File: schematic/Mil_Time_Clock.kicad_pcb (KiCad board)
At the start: 2 copper layers, 188.8 x 102.5 mm, 106 parts, among them J1 Conn_01x27, J2 Speaker_Conn_01x02, J3 Barrel_Jack_Switch, J4 Conn_01x27, Q1 2N3904, Q2 2N3904, Q3 2N3904, Q4 2N3904, Q5 2N3904, U1 SM420561N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

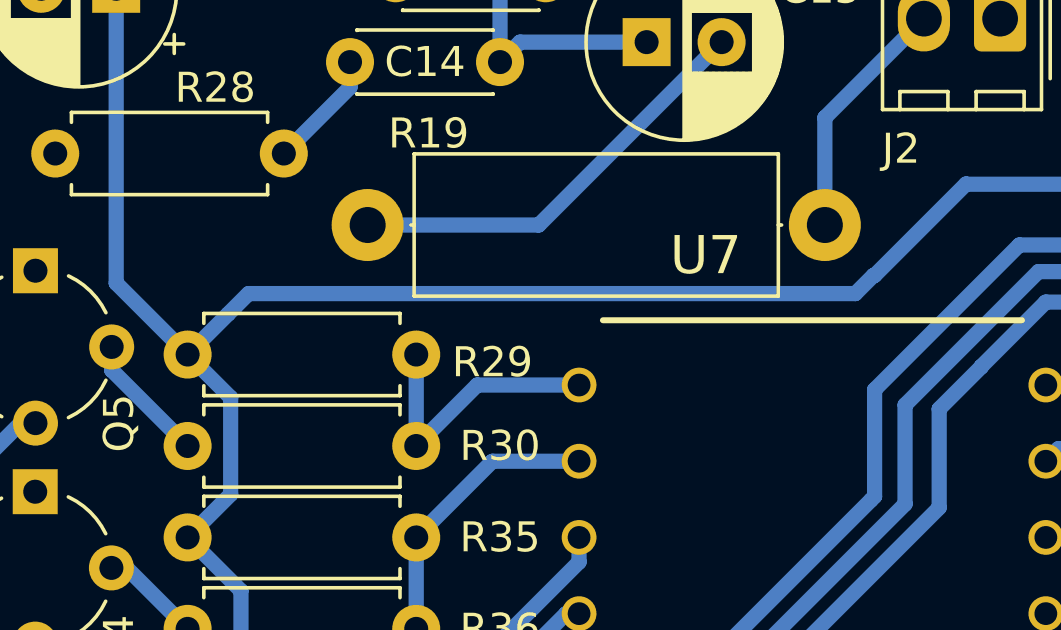
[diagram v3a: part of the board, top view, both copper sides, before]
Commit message: fixed ground issue
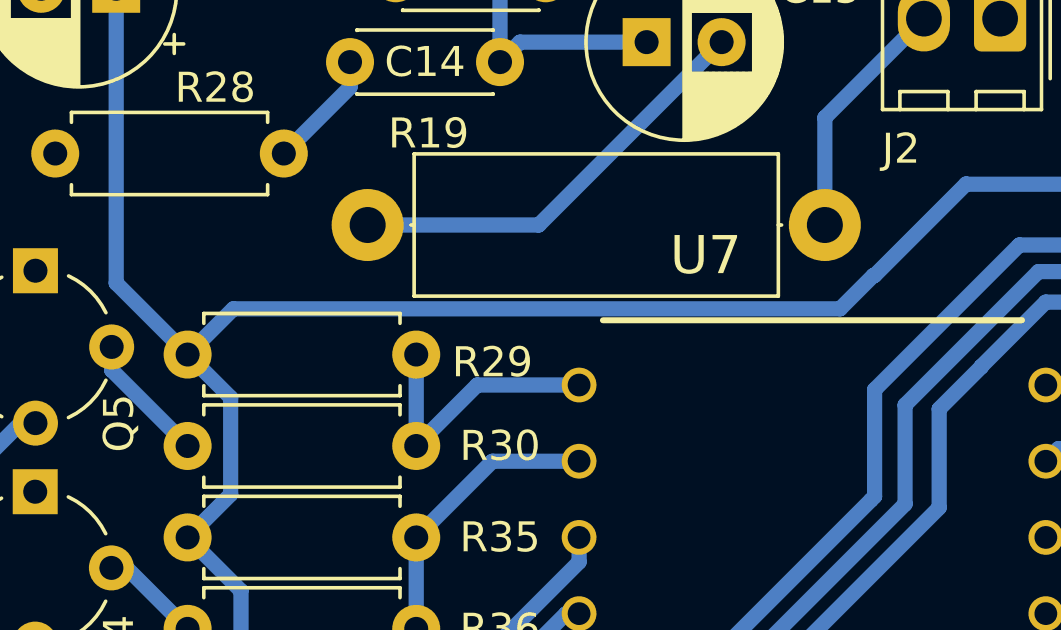
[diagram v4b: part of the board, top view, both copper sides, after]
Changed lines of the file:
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@@
   (via (at 118.11 99.568) (size 1.524) (drill 0.8128) (layers "F.Cu" "B.Cu") (net 4))
   (segment (start 168.716578 118.023894) (end 168.716578 104.841422) (width 0.508) (layer "B.Cu") (net 4))
+  (segment (start 111.777323 39.988604) (end 109.2595 42.506427) (width 0.508) (layer "B.Cu") (net 4))
   (segment (start 77.978 89.662) (end 74.93 86.614) (width 0.508) (layer "B.Cu") (net 4))
   (segment (start 91.599 97.536) (end 91.948 97.187) (width 0.508) (layer "B.Cu") (net 4))
@@
   (segment (start 86.106 97.536) (end 84.963 97.536) (width 0.508) (layer "B.Cu") (net 4))
   (segment (start 74.333 69.431) (end 72.898 70.866) (width 0.508) (layer "B.Cu") (net 4))
-  (segment (start 111.777323 39.878) (end 111.777323 39.988604) (width 0.508) (layer "B.Cu") (net 4))
+  (segment (start 98.853281 59.093) (end 98.8455 59.085219) (width 0.508) (layer "B.Cu") (net 4))
   (segment (start 79.875 46.188) (end 77.375 46.188) (width 0.508) (layer "B.Cu") (net 4))
+  (segment (start 106.203719 59.093) (end 98.853281 59.093) (width 0.508) (layer "B.Cu") (net 4))
   (segment (start 88.9 94.139) (end 85.947 91.186) (width 0.508) (layer "B.Cu") (net 4))
   (segment (start 74.93 85.09) (end 72.898 83.058) (width 0.508) (layer "B.Cu") (net 4))
@@
   (segment (start 98.044 127.508) (end 93.472 122.936) (width 0.508) (layer "B.Cu") (net 4))
   (segment (start 81.28 91.44) (end 79.502 89.662) (width 0.508) (layer "B.Cu") (net 4))
-  (segment (start 109.2595 42.506427) (end 109.2595 48.671219) (width 0.508) (layer "B.Cu") (net 4))
   (segment (start 82.963 49.276) (end 79.875 46.188) (width 0.508) (layer "B.Cu") (net 4))
   (segment (start 74.676 75.184) (end 72.898 76.962) (width 0.508) (layer "B.Cu") (net 4))
@@
   (segment (start 134.366 81.788) (end 134.366 78.994) (width 0.508) (layer "B.Cu") (net 4))
   (segment (start 104.14 98.766) (end 104.14 97.183437) (width 0.508) (layer "B.Cu") (net 4))
+  (segment (start 95.759781 62.133219) (end 94.647 63.246) (width 0.508) (layer "B.Cu") (net 4))
   (segment (start 136.652 58.46) (end 131.652 63.46) (width 0.508) (layer "B.Cu") (net 4))
   (segment (start 93.472 122.936) (end 89.916 122.936) (width 0.508) (layer "B.Cu") (net 4))
@@
   (segment (start 91.853 114.046) (end 91.948 114.141) (width 0.508) (layer "B.Cu") (net 4))
   (segment (start 79.502 89.662) (end 77.978 89.662) (width 0.508) (layer "B.Cu") (net 4))
+  (segment (start 94.647 63.246) (end 74.422 63.246) (width 0.508) (layer "B.Cu") (net 4))
   (segment (start 85.693 91.44) (end 85.947 91.186) (width 0.508) (layer "B.Cu") (net 4))
   (segment (start 72.898 64.77) (end 74.333 66.205) (width 0.508) (layer "B.Cu") (net 4))
@@
   (segment (start 85.947 114.046) (end 91.853 114.046) (width 0.508) (layer "B.Cu") (net 4))
   (segment (start 209.229578 101.386894) (end 209.230058 101.387374) (width 0.508) (layer "B.Cu") (net 4))
-  (segment (start 98.8455 59.085219) (end 95.7975 62.133219) (width 0.508) (layer "B.Cu") (net 4))
   (segment (start 104.14 98.766) (end 108.672 98.766) (width 0.508) (layer "B.Cu") (net 4))
-  (segment (start 95.7975 62.133219) (end 95.759781 62.133219) (width 0.508) (layer "B.Cu") (net 4))
   (segment (start 70.517 52.578) (end 70.517 62.389) (width 0.508) (layer "B.Cu") (net 4))
   (segment (start 104.14 97.183437) (end 102.008063 95.0515) (width 0.508) (layer "B.Cu") (net 4))
@@
   (segment (start 221.083378 99.547954) (end 229.676578 99.547954) (width 0.508) (layer "B.Cu") (net 4))
   (segment (start 131.064 75.692) (end 131.064 63.46) (width 0.508) (layer "B.Cu") (net 4))
+  (segment (start 106.9735 58.323219) (end 106.203719 59.093) (width 0.508) (layer "B.Cu") (net 4))
   (segment (start 114.554 99.568) (end 118.11 99.568) (width 0.508) (layer "B.Cu") (net 4))
   (segment (start 109.474 99.568) (end 114.554 99.568) (width 0.508) (layer "B.Cu") (net 4))
-  (segment (start 95.155 62.738) (end 74.93 62.738) (width 0.508) (layer "B.Cu") (net 4))
   (segment (start 187.713778 101.207094) (end 187.852684 101.346) (width 0.508) (layer "B.Cu") (net 4))
   (segment (start 77.375 47.812888) (end 76.105 49.082888) (width 0.508) (layer "B.Cu") (net 4))
+  (segment (start 95.7975 62.133219) (end 95.759781 62.133219) (width 0.508) (layer "B.Cu") (net 4))
   (segment (start 75.311 113.538) (end 75.311 95.25) (width 0.508) (layer "B.Cu") (net 4))
   (segment (start 161.863578 121.320894) (end 163.382578 119.801894) (width 0.508) (layer "B.Cu") (net 4))
@@
   (segment (start 108.672 98.766) (end 109.474 99.568) (width 0.508) (layer "B.Cu") (net 4))
   (segment (start 89.8125 95.0515) (end 88.9 94.139) (width 0.508) (layer "B.Cu") (net 4))
-  (segment (start 106.203719 59.093) (end 98.853281 59.093) (width 0.508) (layer "B.Cu") (net 4))
   (segment (start 131.652 63.46) (end 131.064 63.46) (width 0.508) (layer "B.Cu") (net 4))
   (segment (start 221.083378 101.217094) (end 221.083378 99.547954) (width 0.508) (layer "B.Cu") (net 4))
+  (segment (start 106.9735 50.957219) (end 106.9735 58.323219) (width 0.508) (layer "B.Cu") (net 4))
   (segment (start 91.3512 117.1828) (end 91.3512 121.5008) (width 0.508) (layer "B.Cu") (net 4))
   (segment (start 91.948 116.586) (end 91.3512 117.1828) (width 0.508) (layer "B.Cu") (net 4))
-  (segment (start 74.2475 63.4205) (end 72.898 64.77) (width 0.508) (layer "B.Cu") (net 4))
+  (segment (start 111.777323 39.878) (end 111.777323 39.988604) (width 0.508) (layer "B.Cu") (net 4))
+  (segment (start 98.8455 59.085219) (end 95.7975 62.133219) (width 0.508) (layer "B.Cu") (net 4))
   (segment (start 201.777472 127.196894) (end 201.736578 127.156) (width 0.508) (layer "B.Cu") (net 4))
   (segment (start 70.517 62.389) (end 72.898 64.77) (width 0.508) (layer "B.Cu") (net 4))
   (segment (start 166.938578 119.801894) (end 168.716578 118.023894) (width 0.508) (layer "B.Cu") (net 4))
   (segment (start 134.366 96.52) (end 134.366 81.788) (width 0.508) (layer "B.Cu") (net 4))
-  (segment (start 106.9735 50.957219) (end 106.9735 58.323219) (width 0.508) (layer "B.Cu") (net 4))
   (segment (start 91.948 114.141) (end 91.948 97.187) (width 0.508) (layer "B.Cu") (net 4))
   (segment (start 161.863578 123.35013) (end 170.468342 131.954894) (width 0.508) (layer "B.Cu") (net 4))
   (segment (start 77.375 46.188) (end 70.4535 46.188) (width 0.508) (layer "B.Cu") (net 4))
-  (segment (start 111.777323 39.988604) (end 109.2595 42.506427) (width 0.508) (layer "B.Cu") (net 4))
   (segment (start 114.808 39.878) (end 111.777323 39.878) (width 0.508) (layer "B.Cu") (net 4))
-  (segment (start 95.759781 62.133219) (end 95.155 62.738) (width 0.508) (layer "B.Cu") (net 4))
   (segment (start 168.716578 104.841422) (end 172.212 101.346) (width 0.508) (layer "B.Cu") (net 4))
-  (segment (start 109.2595 48.671219) (end 106.9735 50.957219) (width 0.508) (layer "B.Cu") (net 4))
   (segment (start 72.898 70.866) (end 74.676 72.644) (width 0.508) (layer "B.Cu") (net 4))
   (segment (start 134.366 99.568) (end 134.366 96.52) (width 0.508) (layer "B.Cu") (net 4))
+  (segment (start 109.2595 42.506427) (end 109.2595 48.671219) (width 0.508) (layer "B.Cu") (net 4))
   (segment (start 74.676 72.644) (end 74.676 75.184) (width 0.508) (layer "B.Cu") (net 4))
   (segment (start 198.836978 99.547954) (end 198.836978 100.857494) (width 0.508) (layer "B.Cu") (net 4))
+  (segment (start 109.2595 48.671219) (end 106.9735 50.957219) (width 0.508) (layer "B.Cu") (net 4))
   (segment (start 198.307578 101.386894) (end 209.229578 101.386894) (width 0.508) (layer "B.Cu") (net 4))
   (segment (start 199.235578 131.954894) (end 200.720578 130.469894) (width 0.508) (layer "B.Cu") (net 4))
+  (segment (start 74.422 63.246) (end 72.898 64.77) (width 0.508) (layer "B.Cu") (net 4))
   (segment (start 161.863578 122.537924) (end 161.863578 123.35013) (width 0.508) (layer "B.Cu") (net 4))
   (segment (start 91.3512 121.5008) (end 89.916 122.936) (width 0.508) (layer "B.Cu") (net 4))
@@
   (segment (start 102.008063 95.0515) (end 89.8125 95.0515) (width 0.508) (layer "B.Cu") (net 4))
   (segment (start 201.736578 129.453894) (end 200.720578 130.469894) (width 0.508) (layer "B.Cu") (net 4))
-  (segment (start 74.93 62.738) (end 74.2475 63.4205) (width 0.508) (layer "B.Cu") (net 4))
   (segment (start 74.333 78.397) (end 74.333 81.623) (width 0.508) (layer "B.Cu") (net 4))
-  (segment (start 106.9735 58.323219) (end 106.203719 59.093) (width 0.508) (layer "B.Cu") (net 4))
-  (segment (start 98.853281 59.093) (end 98.8455 59.085219) (width 0.508) (layer "B.Cu") (net 4))
   (segment (start 134.366 78.994) (end 131.064 75.692) (width 0.508) (layer "B.Cu") (net 4))
   (segment (start 168.931079 133.732395) (end 158.169578 122.970894) (width 0.508) (layer "B.Cu") (net 5))

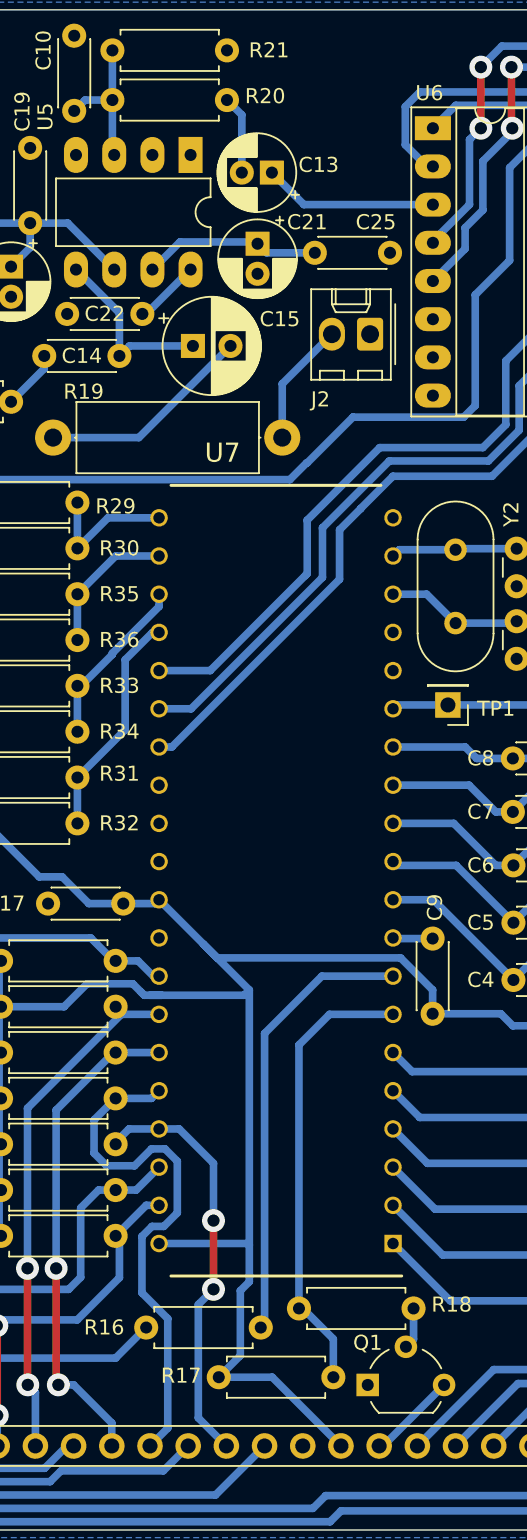
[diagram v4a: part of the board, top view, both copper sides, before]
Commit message: added resistor from input to bypass of lm386. When the alarm is off the input is ground, this reduces noise issues to about nothing. Updated PCB.
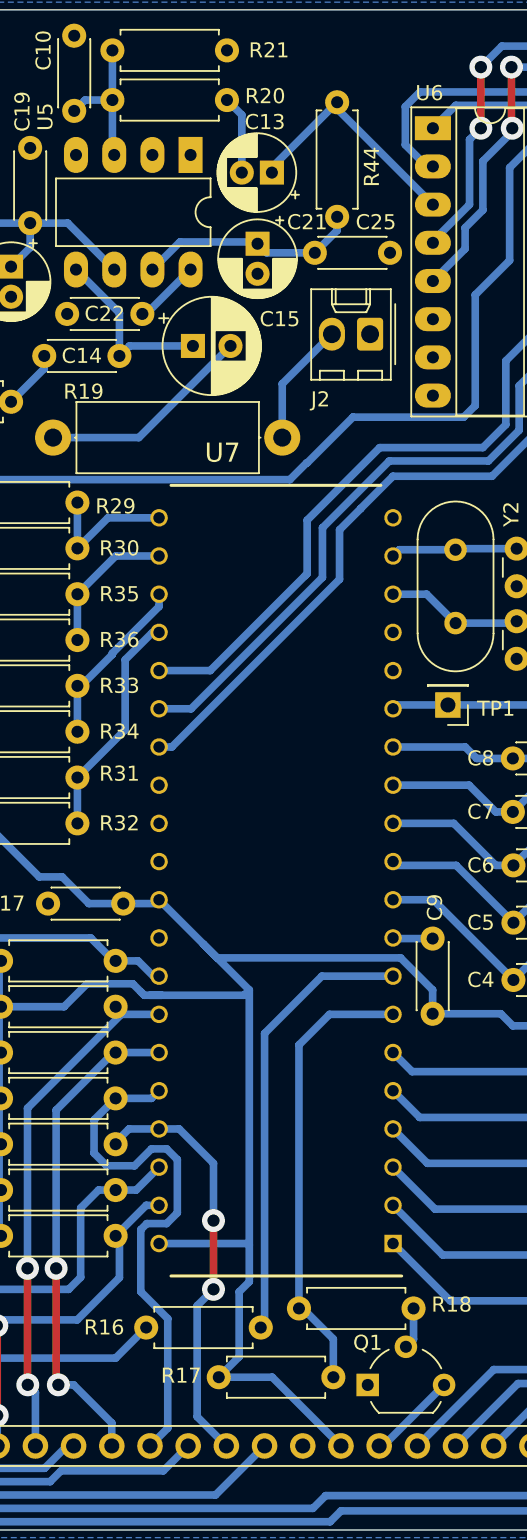
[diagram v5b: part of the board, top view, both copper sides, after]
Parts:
- added R44: 470R, Resistor_THT:R_Axial_DIN0207_L6.3mm_D2.5mm_P7.62mm_Horizontal, F.Cu at (97.8, 45.8)
- C2: value 6-30pF -> 2-5pF
- C26: value 18pF -> 8pF
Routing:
- net Net-(U6-A): track 11.6 -> 15.9 mm
- net Net-(U5-BYPASS): track 11.7 -> 14.7 mm
